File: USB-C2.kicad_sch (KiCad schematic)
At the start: 91 parts, among them J4 USB_C_Receptacle, J5 I2C2_PD_Controller, J6 I2C_Mux, J7 I2C_EEPROM, SW2 FW_Upgrade, U10 24LC256, U11 TPD4E02B04DQA, U12 TPD4E02B04DQA, U13 TPD4E02B04DQA, U14 TUSB1142IRNQR_C5216209, U8 TVS2200DRV, U9 TPS25762CQRQLRQ1

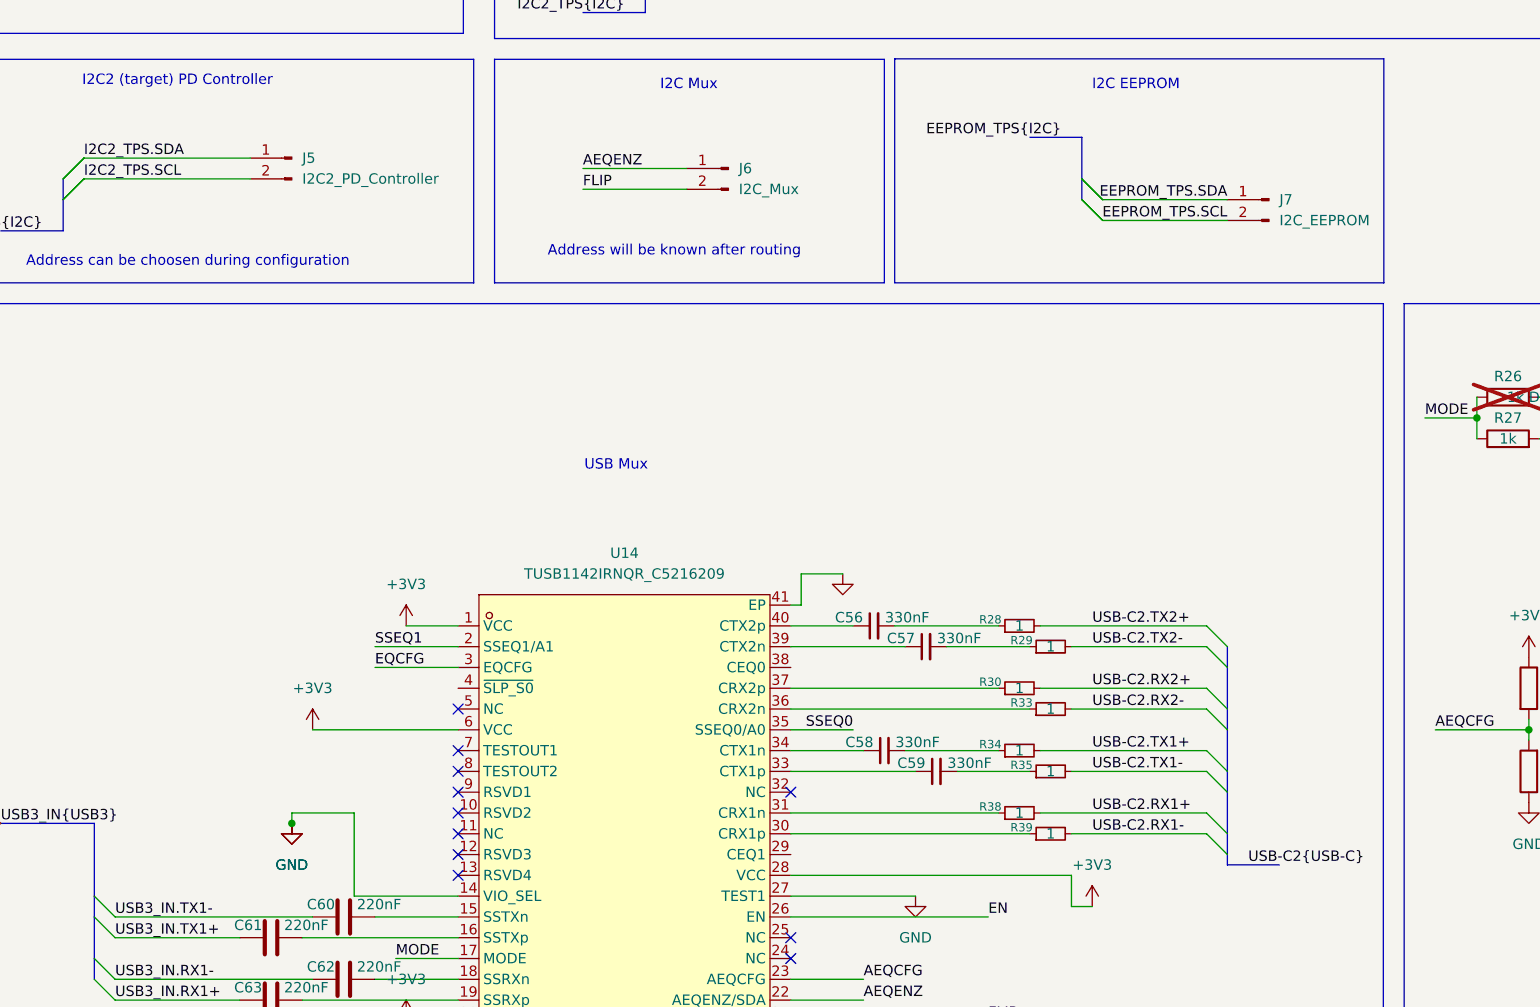
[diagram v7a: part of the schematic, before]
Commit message: Ferrite Breads added for 5V, TVS and ESD diodes added
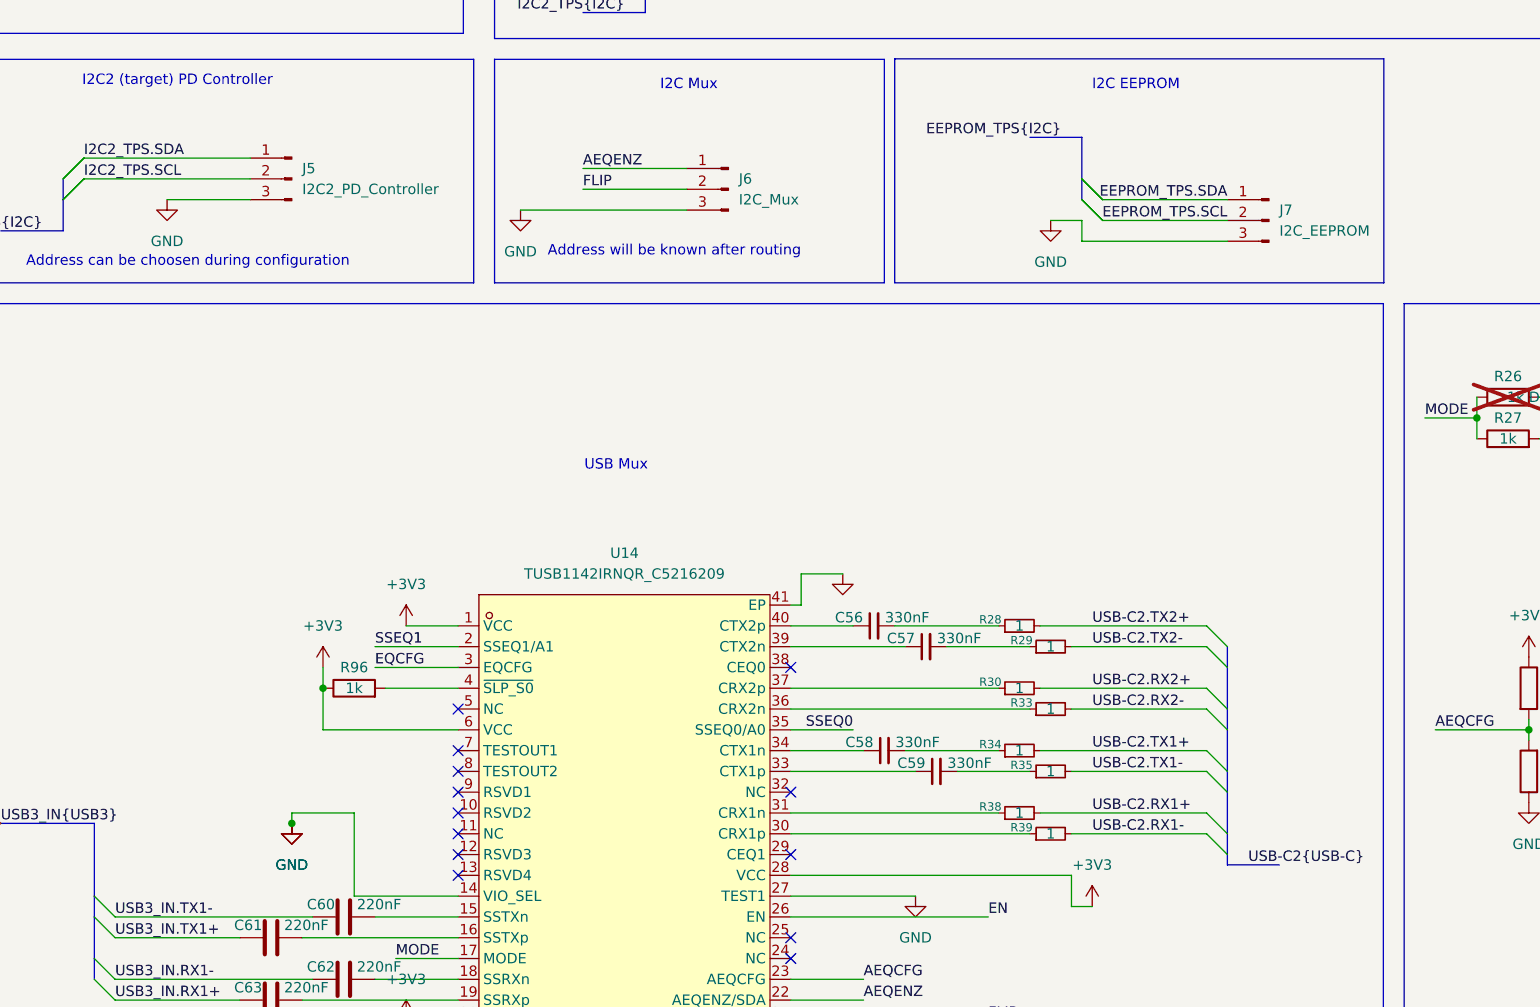
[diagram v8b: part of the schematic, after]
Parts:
- added R96: 1k, Resistor_SMD:R_0402_1005Metric, symbol Device:R
- J5, J6, J7: symbol Connector:Conn_01x02_Pin -> Connector:Conn_01x03_Pin
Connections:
- net +3V3: now also R96.1
- net GND: now also J5.3 (Pin_3), J6.3 (Pin_3), J7.3 (Pin_3)
- net at U14.4 (~{SLP_S0}): now also R96.2
- no-connect marks 14 -> 16
